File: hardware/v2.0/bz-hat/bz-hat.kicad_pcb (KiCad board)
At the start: 2 copper layers, 140 x 85 mm, 61 parts, among them J1 LineIN, J2 LineOUT, J3 Headphones, J4 Raspberry_Pi_4, J5 CVs+CLK_connector, J6 NHD-2.23-12832UCB3, SW1 BTN_f, SW2 BTN_big, SW3 BTN_1, SW4 BTN_2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

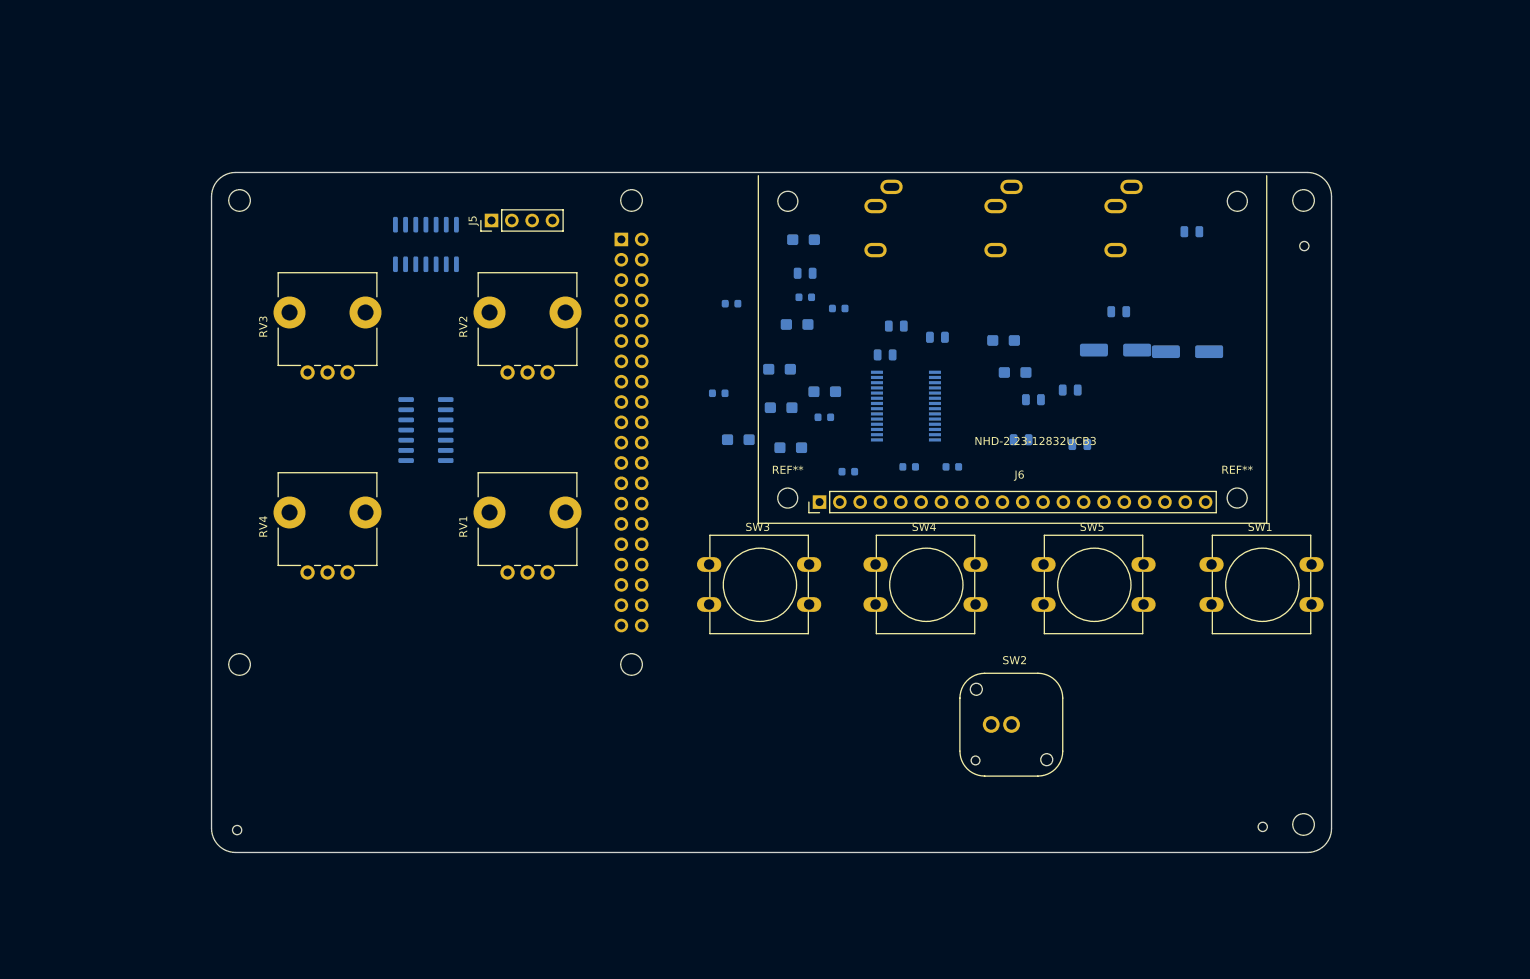
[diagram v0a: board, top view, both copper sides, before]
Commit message: v2 board placement and routing finished
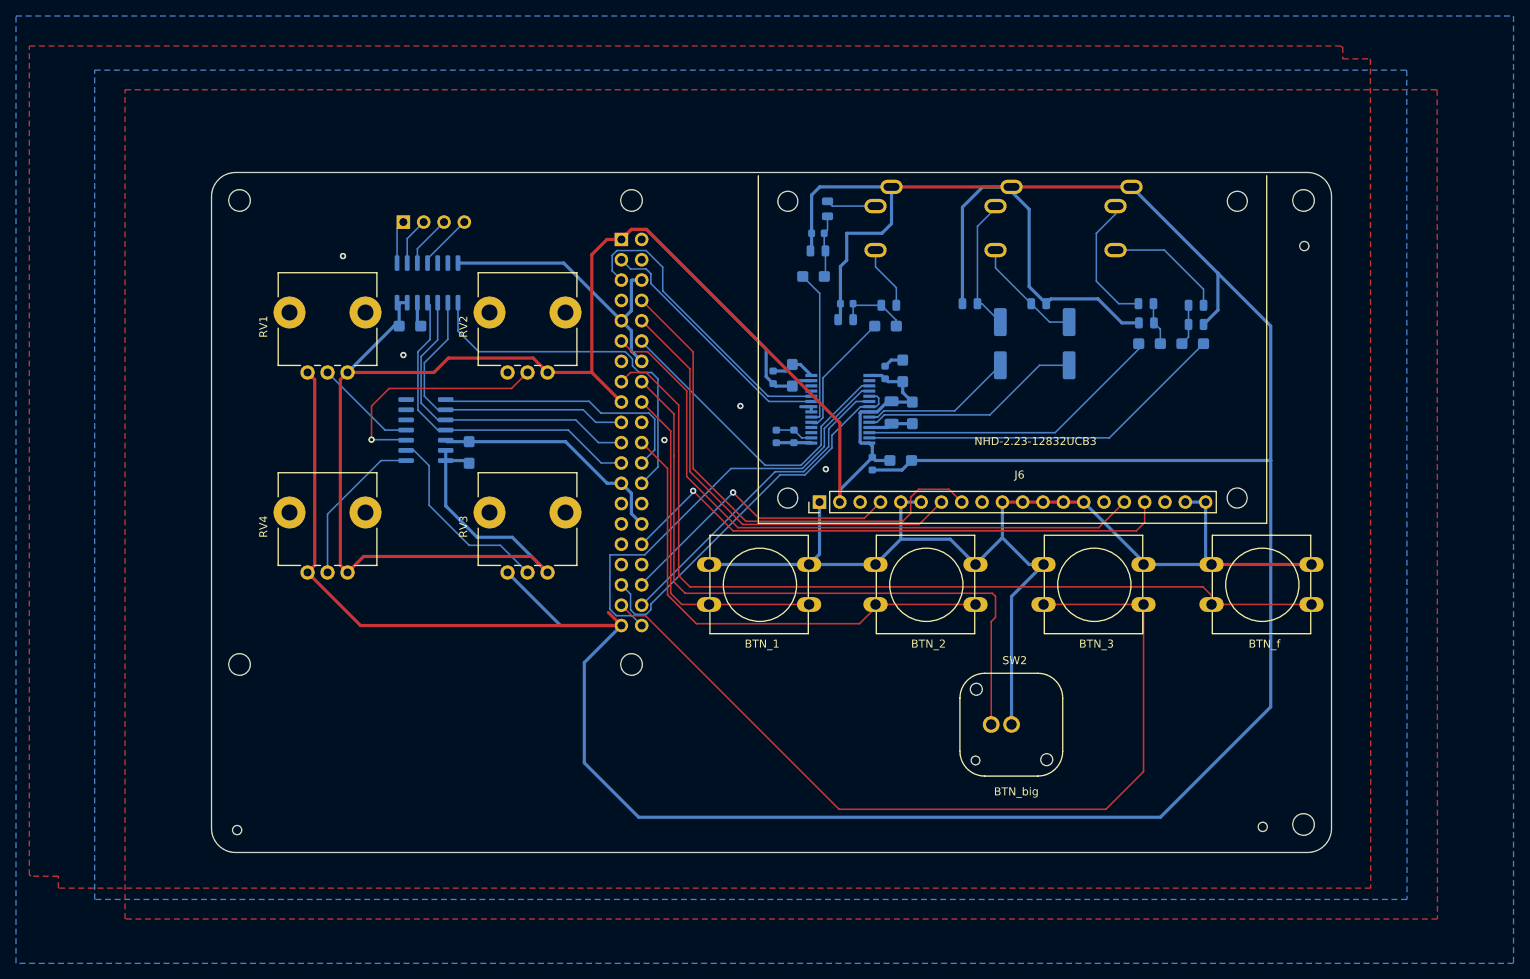
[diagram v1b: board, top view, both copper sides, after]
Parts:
- added C20: 1uF, Capacitor_Tantalum_SMD:CP_EIA-3216-18_Kemet-A, B.Cu at (112.2, 80.0)
- C13: footprint Capacitor_SMD:C_0603_1608Metric -> Capacitor_SMD:C_1206_3216Metric
- C18: footprint Capacitor_SMD:C_0603_1608Metric -> Capacitor_Tantalum_SMD:CP_EIA-3216-18_Kemet-A
- C19: footprint Capacitor_Tantalum_SMD:CP_EIA-3216-18_Kemet-A -> Capacitor_SMD:C_0603_1608Metric
- J5: moved to B.Cu
- moved C18 40.3 mm to (104.8, 64.2)
- moved RV1 35.4 mm to (97.0, 70.0)
- moved RV3 35.4 mm to (122.0, 95.0)
- moved R4 27.6 mm to (203.1, 61.6)
- moved C4 23.7 mm to (202.7, 66.4), turned to 180 degrees
- moved R8 22.4 mm to (203.1, 64.0)
- moved C10 22.0 mm to (167.6, 75.0), turned to 270 degrees
- moved R10 21.1 mm to (183.4, 61.4)
- moved C14 21.1 mm to (162.6, 81.4), turned to 270 degrees
- moved R3 19.4 mm to (196.8, 61.4), turned to 180 degrees
- moved C11 19.0 mm to (166.2, 81.0)
- moved R9 18.6 mm to (174.8, 61.4)
- moved R5 18.4 mm to (155.8, 54.8)
- moved C3 17.2 mm to (197.2, 66.4)
- moved C9 17.0 mm to (166.4, 69.8), turned to 90 degrees
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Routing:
- net GNDA: track 0.00 -> 492.9 mm, vias 0 -> 2
- net +3V3: track 0.00 -> 261.7 mm
- net GNDD: track 0.00 -> 188.8 mm, vias 0 -> 3
- net /BTN_f: track 0.00 -> 111.9 mm
- net /BTN_3: track 0.00 -> 111.2 mm
- net /BTN_big: track 0.00 -> 83.9 mm
- net /D_RES: track 0.00 -> 80.1 mm
- net /D_CE: track 0.00 -> 70.8 mm, vias 0 -> 1
- net /D_MOSI: track 0.00 -> 63.5 mm
- net /BTN_2: track 0.00 -> 61.6 mm
- net /D_SCLK: track 0.00 -> 56.7 mm
- net /DACDAT: track 0.00 -> 53.9 mm
- net /LRC: track 0.00 -> 50.0 mm
- net /ROUT: track 0.00 -> 46.7 mm
- net /SPI0_CS1: track 0.00 -> 45.4 mm
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- added copper zone on B.Cu, net GNDA
- added copper zone on F.Cu, net GNDA
- added copper zone on B.Cu, net GNDD
- added copper zone on F.Cu, net GNDD

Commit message: logo + gerbers + JLPCB refs. to symbols
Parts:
- added G***: LOGO, custom:logo, F.Cu at (107.8, 112.0)
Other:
- board text added: "pi4"
- board text added: "sombrero"

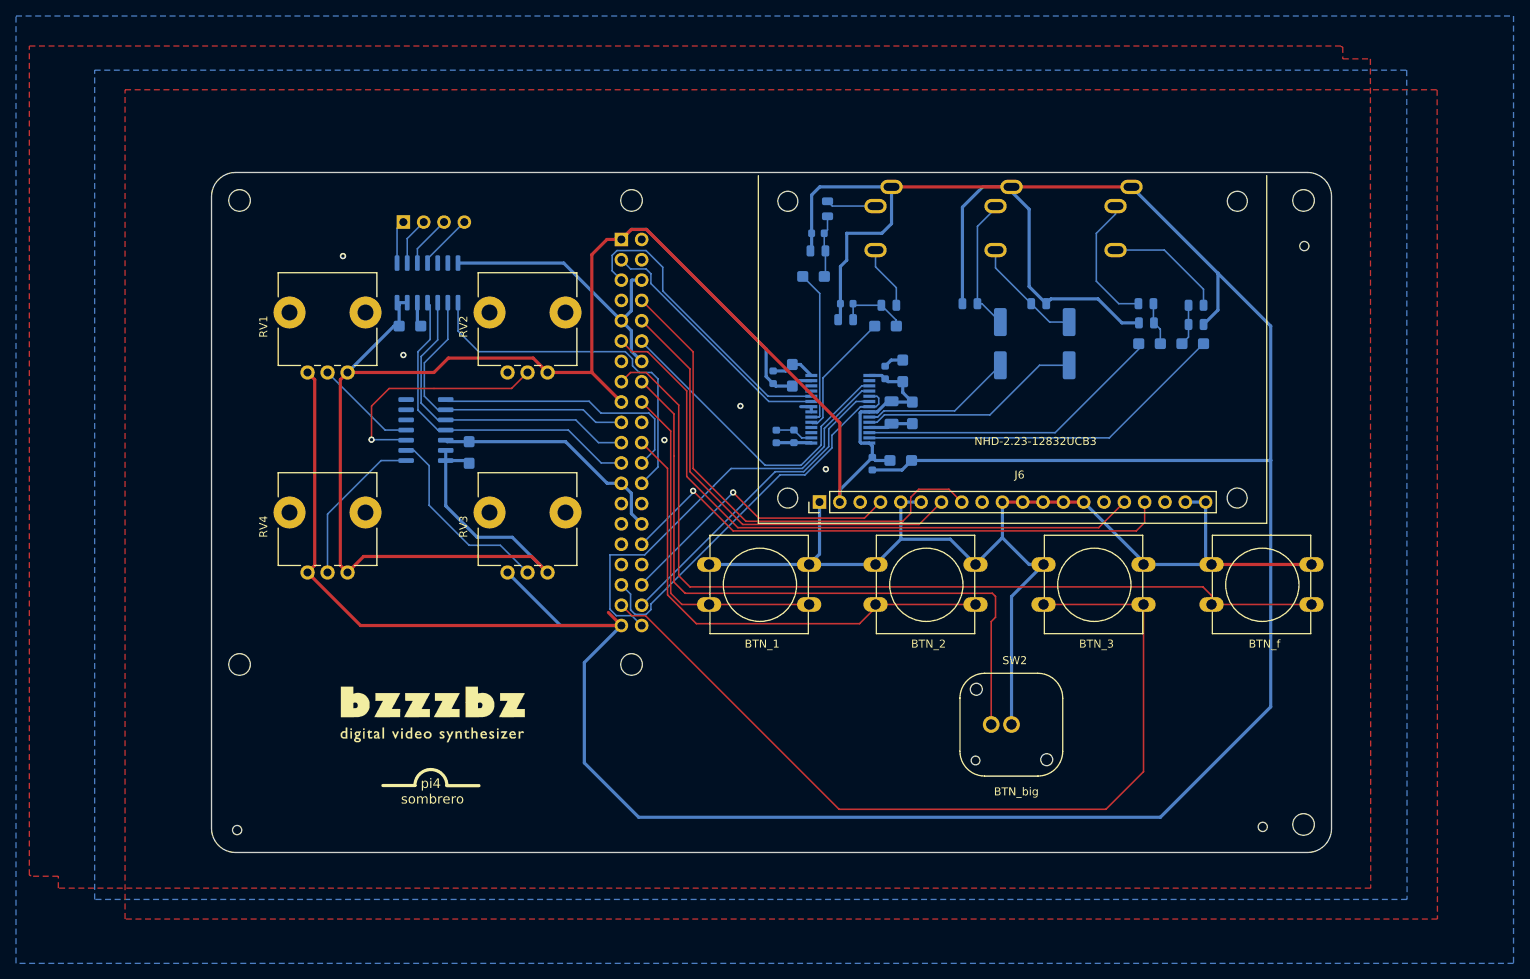
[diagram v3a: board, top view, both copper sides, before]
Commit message: Fixed C19 wrong footprint
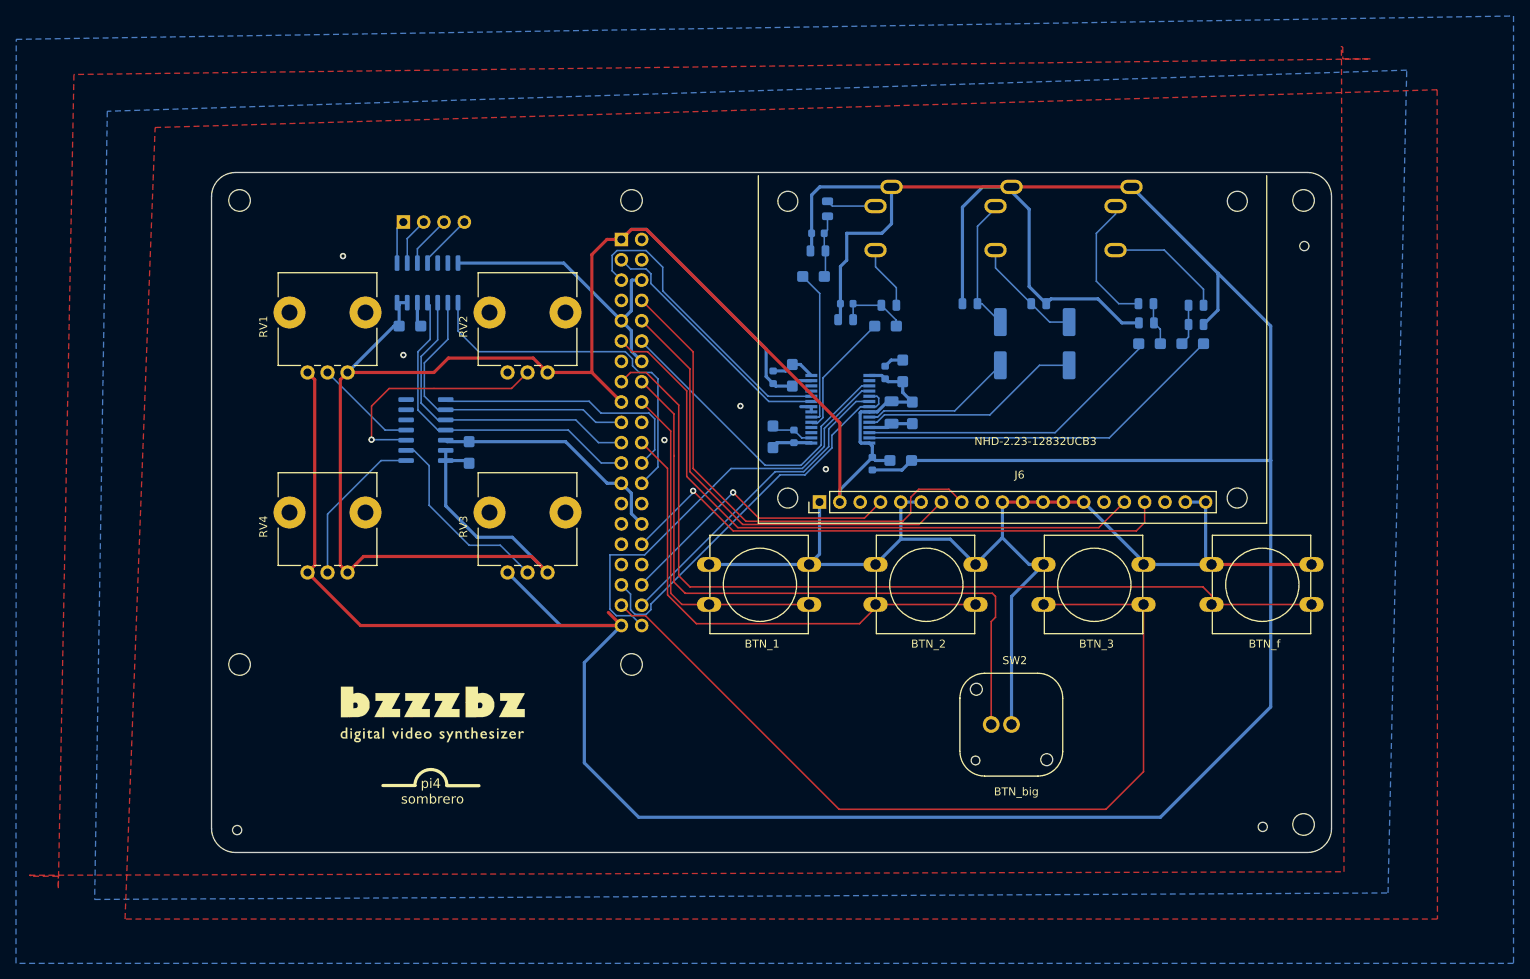
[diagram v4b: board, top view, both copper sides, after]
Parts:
- C19: footprint Capacitor_SMD:C_0603_1608Metric -> Capacitor_Tantalum_SMD:CP_EIA-3216-18_Kemet-A
- moved C19 0.42 mm to (150.2, 78.0)
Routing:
- net GNDA: track 492.9 -> 493.6 mm
- net Net-(C16-Pad2): track 4.78 -> 5.41 mm
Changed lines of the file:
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@@
     (thickness 1.6)
     (drawings 13)
-    (tracks 448)
+    (tracks 450)
     (zones 0)
     (modules 63)
@@
   (page A4)
   (layers
-    (0 F.Cu signal hide)
-    (31 B.Cu signal hide)
+    (0 F.Cu signal)
+    (31 B.Cu signal)
     (32 B.Adhes user)
     (33 F.Adhes user)
@@
       (drillshape 0)
       (scaleselection 1)
-      (outputdirectory ""))
+      (outputdirectory "gerber_corrected"))
   )
   (net 0 "")
@@
     (add_net GNDD)
   )
+  (module Capacitor_Tantalum_SMD:CP_EIA-3216-18_Kemet-A (layer B.Cu)
+    (at 150.18 78.04 270)
+    (descr "Tantalum Capacitor SMD Kemet-A (3216-18 Metric), IPC_7351 nominal, (Body size from: http://www.kemet.com/Lists/ProductCatalog/Attachments/253/KEM_TC101_STD.pdf), generated with kicad-footprint-generator")
+    (tags "capacitor tantalum")
+    (attr smd)
+    (fp_text reference C19 (at 0 1.75 90) (layer B.SilkS)
+      (effects (font (size 1 1) (thickness 0.15)) (justify mirror))
+    )
+    (fp_text value 10uF (at 0 -1.75 90) (layer B.Fab)
+      (effects (font (size 1 1) (thickness 0.15)) (justify mirror))
+    )
+    (fp_line (start 2.3 -1.05) (end -2.3 -1.05) (layer B.CrtYd) (width 0.05))
+    (fp_line (start 2.3 1.05) (end 2.3 -1.05) (layer B.CrtYd) (width 0.05))
+    (fp_line (start -2.3 1.05) (end 2.3 1.05) (layer B.CrtYd) (width 0.05))
+    (fp_line (start -2.3 -1.05) (end -2.3 1.05) (layer B.CrtYd) (width 0.05))
+    (fp_line (start -2.31 -0.935) (end 1.6 -0.935) (layer B.SilkS) (width 0.12))
+    (fp_line (start -2.31 0.935) (end -2.31 -0.935) (layer B.SilkS) (width 0.12))
+    (fp_line (start 1.6 0.935) (end -2.31 0.935) (layer B.SilkS) (width 0.12))
+    (fp_line (start 1.6 -0.8) (end 1.6 0.8) (layer B.Fab) (width 0.1))
+    (fp_line (start -1.6 -0.8) (end 1.6 -0.8) (layer B.Fab) (width 0.1))
+    (fp_line (start -1.6 0.4) (end -1.6 -0.8) (layer B.Fab) (width 0.1))
+    (fp_line (start -1.2 0.8) (end -1.6 0.4) (layer B.Fab) (width 0.1))
+    (fp_line (start 1.6 0.8) (end -1.2 0.8) (layer B.Fab) (width 0.1))
+    (fp_text user %R (at 0 0 90) (layer B.Fab)
+      (effects (font (size 0.8 0.8) (thickness 0.12)) (justify mirror))
+    )
+    (pad 2 smd roundrect (at 1.35 0 270) (size 1.4 1.35) (layers B.Cu B.Paste B.Mask) (roundrect_rratio 0.185185)
+      (net 1 GNDA))
+    (pad 1 smd roundrect (at -1.35 0 270) (size 1.4 1.35) (layers B.Cu B.Paste B.Mask) (roundrect_rratio 0.185185)
+      (net 16 "Net-(C16-Pad2)"))
+    (model ${KISYS3DMOD}/Capacitor_Tantalum_SMD.3dshapes/CP_EIA-3216-18_Kemet-A.wrl
+      (at (xyz 0 0 0))
+      (scale (xyz 1 1 1))
+      (rotate (xyz 0 0 0))
+    )
+  )
   (module custom:logo (layer F.Cu)
     (at 107.78 112)
@@
     )
   )
-  (module Capacitor_SMD:C_0603_1608Metric (layer B.Cu)
-    (at 150.6 78 270)
-    (descr "Capacitor SMD 0603 (1608 Metric), square (rectangular) end terminal, IPC_7351 nominal, (Body size source: http://www.tortai-tech.com/upload/download/2011102023233369053.pdf), generated with kicad-footprint-generator")
-    (tags capacitor)
-    (attr smd)
-    (fp_text reference C19 (at 0.16 2.4 180) (layer B.SilkS)
-      (effects (font (size 1 1) (thickness 0.15)) (justify mirror))
-    )
-    (fp_text value 10uF (at 0 -1.43 90) (layer B.Fab)
-      (effects (font (size 1 1) (thickness 0.15)) (justify mirror))
-    )
-    (fp_line (start 1.48 -0.73) (end -1.48 -0.73) (layer B.CrtYd) (width 0.05))
-    (fp_line (start 1.48 0.73) (end 1.48 -0.73) (layer B.CrtYd) (width 0.05))
-    (fp_line (start -1.48 0.73) (end 1.48 0.73) (layer B.CrtYd) (width 0.05))
-    (fp_line (start -1.48 -0.73) (end -1.48 0.73) (layer B.CrtYd) (width 0.05))
-    (fp_line (start -0.162779 -0.51) (end 0.162779 -0.51) (layer B.SilkS) (width 0.12))
-    (fp_line (start -0.162779 0.51) (end 0.162779 0.51) (layer B.SilkS) (width 0.12))
-    (fp_line (start 0.8 -0.4) (end -0.8 -0.4) (layer B.Fab) (width 0.1))
-    (fp_line (start 0.8 0.4) (end 0.8 -0.4) (layer B.Fab) (width 0.1))
-    (fp_line (start -0.8 0.4) (end 0.8 0.4) (layer B.Fab) (width 0.1))
-    (fp_line (start -0.8 -0.4) (end -0.8 0.4) (layer B.Fab) (width 0.1))
-    (fp_text user %R (at 0 0 90) (layer B.Fab)
-      (effects (font (size 0.4 0.4) (thickness 0.06)) (justify mirror))
-    )
-    (pad 2 smd roundrect (at 0.7875 0 270) (size 0.875 0.95) (layers B.Cu B.Paste B.Mask) (roundrect_rratio 0.25)
-      (net 1 GNDA))
-    (pad 1 smd roundrect (at -0.7875 0 270) (size 0.875 0.95) (layers B.Cu B.Paste B.Mask) (roundrect_rratio 0.25)
-      (net 16 "Net-(C16-Pad2)"))
-    (model ${KISYS3DMOD}/Capacitor_SMD.3dshapes/C_0603_1608Metric.wrl
-      (at (xyz 0 0 0))
-      (scale (xyz 1 1 1))
-      (rotate (xyz 0 0 0))
-    )
-  )
   (module Capacitor_Tantalum_SMD:CP_EIA-3216-18_Kemet-A (layer B.Cu)
     (at 104.8 64.2)
@@
   (segment (start 152.8 78.775) (end 154.925 78.775) (width 0.4) (layer B.Cu) (net 1))
   (segment (start 150.6125 78.775) (end 150.6 78.7875) (width 0.4) (layer B.Cu) (net 1))
-  (segment (start 152.8 78.775) (end 150.6125 78.775) (width 0.4) (layer B.Cu) (net 1))
   (segment (start 123.63 101.63) (end 131.23 101.63) (width 0.4) (layer B.Cu) (net 1))
   (segment (start 117 95) (end 123.63 101.63) (width 0.4) (layer B.Cu) (net 1))
@@
   (via (at 156.79 82.09) (size 0.8) (drill 0.4) (layers F.Cu B.Cu) (net 1))
   (via (at 146.11 74.19) (size 0.8) (drill 0.4) (layers F.Cu B.Cu) (net 1))
+  (segment (start 150.795 78.775) (end 150.18 79.39) (width 0.4) (layer B.Cu) (net 1))
+  (segment (start 152.8 78.775) (end 150.795 78.775) (width 0.4) (layer B.Cu) (net 1))
   (segment (start 157 52.1875) (end 156.5875 52.6) (width 0.2) (layer B.Cu) (net 2))
   (segment (start 157 50.475) (end 157 52.1875) (width 0.2) (layer B.Cu) (net 2))
@@
   (segment (start 153.775 78.175) (end 152.8 77.2) (width 0.2) (layer B.Cu) (net 16))
   (segment (start 154.975 78.175) (end 153.775 78.175) (width 0.2) (layer B.Cu) (net 16))
-  (segment (start 152.8 77.2) (end 150.6 77.2) (width 0.2) (layer B.Cu) (net 16))
+  (segment (start 150.69 77.2) (end 150.18 76.69) (width 0.2) (layer B.Cu) (net 16))
+  (segment (start 152.8 77.2) (end 150.69 77.2) (width 0.2) (layer B.Cu) (net 16))
   (segment (start 132.54 100.4) (end 133.77 101.63) (width 0.2) (layer B.Cu) (net 17))
   (segment (start 130.6 100.4) (end 132.54 100.4) (width 0.2) (layer B.Cu) (net 17))
@@
     (polygon
       (pts
-        (xy 233.24 138.32) (xy 69.19 138.32) (xy 69.19 34.66) (xy 233.2 34.66)
+        (xy 233.24 138.32) (xy 69.19 138.32) (xy 72.95 39.38) (xy 233.2 34.66)
       )
     )
@@
     (polygon
       (pts
-        (xy 229.44 135.87) (xy 65.39 135.87) (xy 65.39 32.21) (xy 229.4 32.21)
+        (xy 66.97 37.35) (xy 65.39 135.87) (xy 227.06 135.06) (xy 229.4 32.21)
       )
     )
@@
     (polygon
       (pts
-        (xy 221.237374 29.31) (xy 221.407328 29.31) (xy 221.407903 30.8) (xy 224.857328 30.8) (xy 224.897328 134.46)
+        (xy 221.237374 29.31) (xy 221.407328 29.31) (xy 221.407903 30.8) (xy 224.857328 30.8) (xy 62.8 32.75)
         (xy 60.847328 134.46) (xy 60.847328 132.97) (xy 57.397328 132.97) (xy 57.397328 132.85) (xy 57.227328 132.85)
-        (xy 57.227328 29.19) (xy 221.237328 29.19)
+        (xy 221.56 132.41) (xy 221.237328 29.19)
       )
     )
@@
     (polygon
       (pts
-        (xy 242.747992 143.86) (xy 55.557992 143.86) (xy 55.557992 25.44) (xy 242.747992 25.44)
+        (xy 242.747992 143.86) (xy 55.557992 143.86) (xy 55.59 28.36) (xy 242.747992 25.44)
       )
     )
